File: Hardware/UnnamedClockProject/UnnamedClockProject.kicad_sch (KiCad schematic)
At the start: 22 parts, among them J101 CLOCK_OUT, J102 POWER, Q101 2N3904, U104 G3MB-202P, U105 G3MB-202P, U106 G3MB-202P

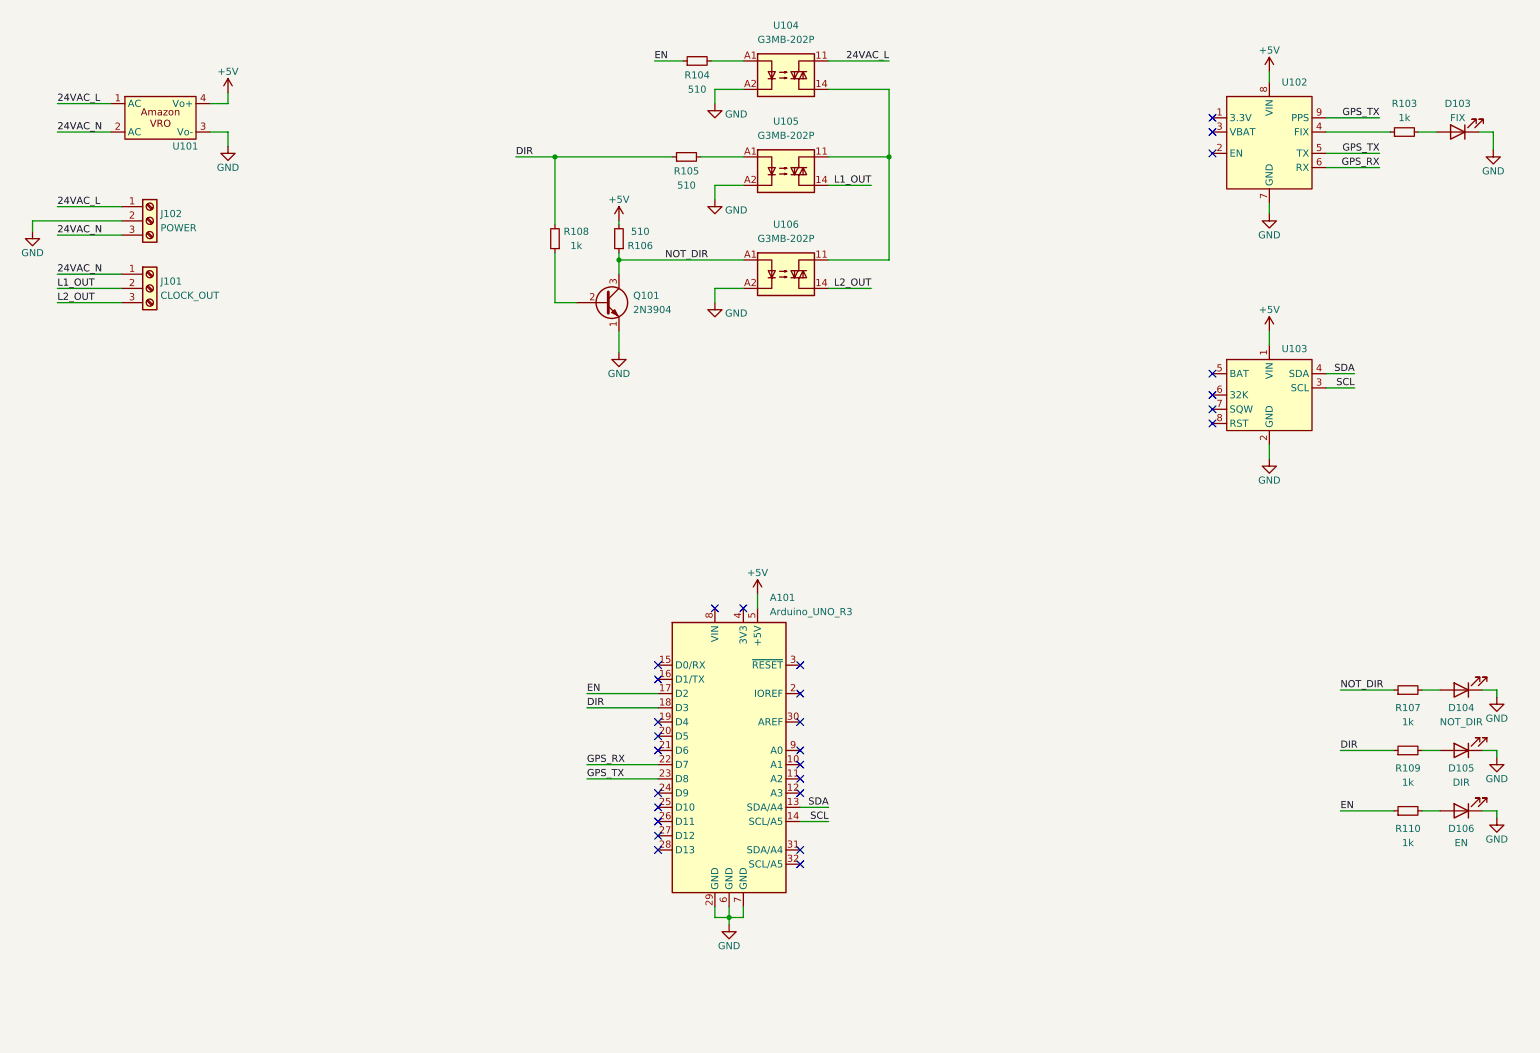
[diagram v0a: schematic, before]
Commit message: Add inital code for LCD
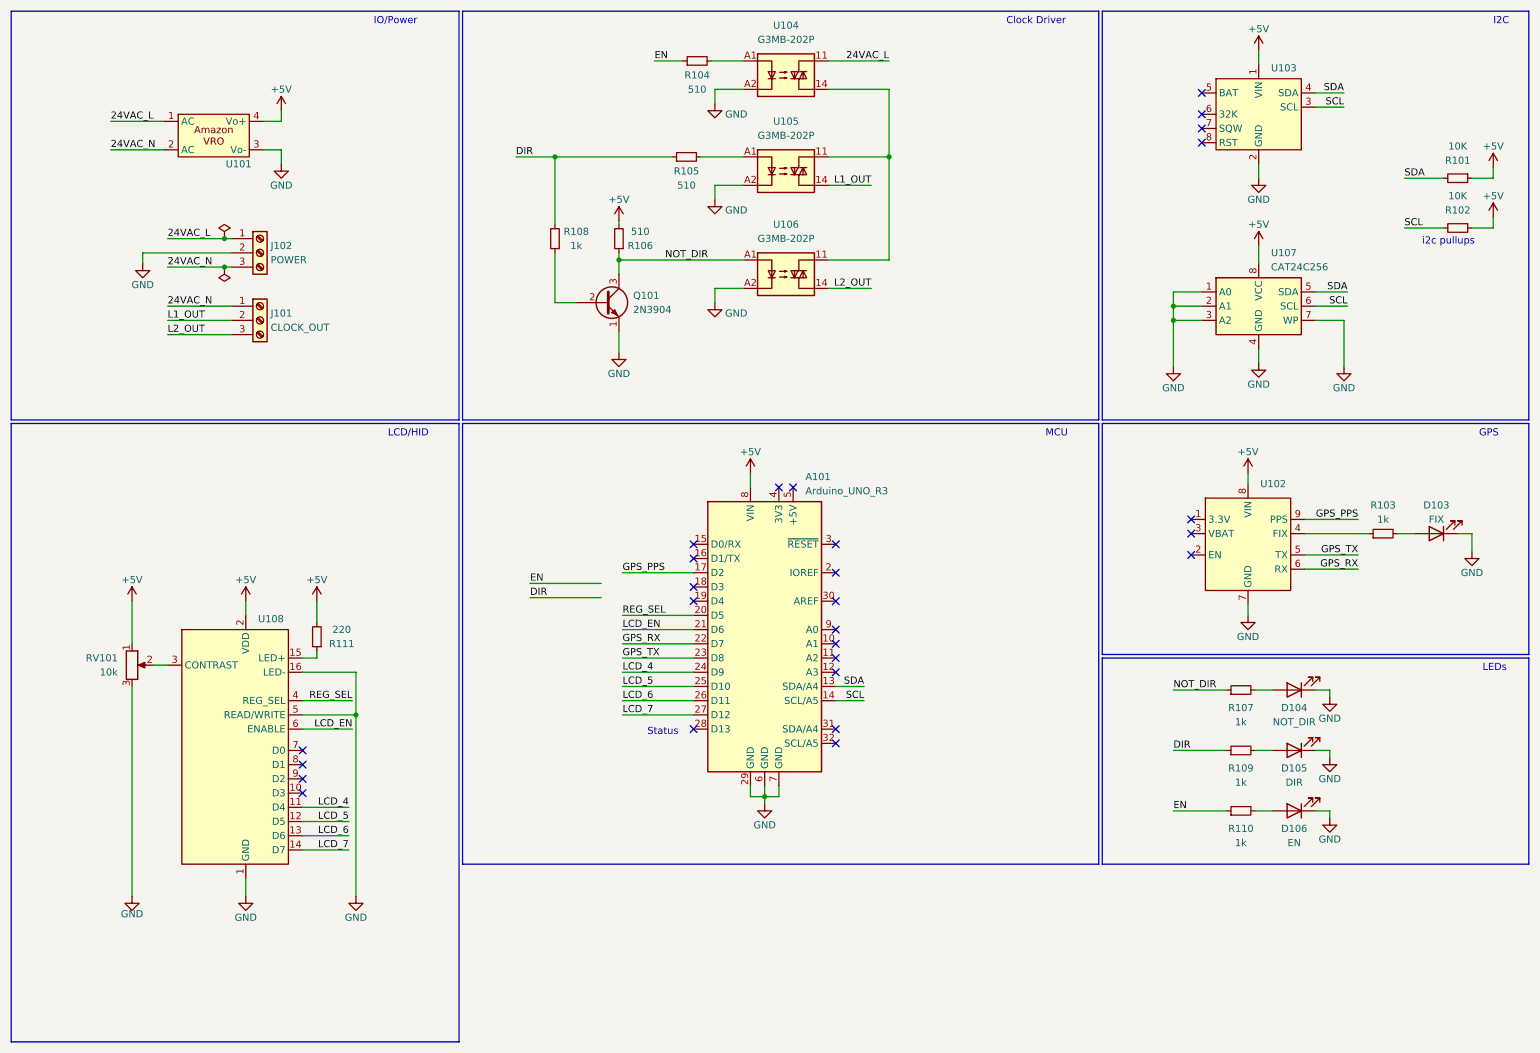
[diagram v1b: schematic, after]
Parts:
- added R101, R102: 10K, Resistor_THT:R_Axial_DIN0207_L6.3mm_D2.5mm_P10.16mm_Horizontal, symbol Device:R_Small
- added R111: 220, Resistor_THT:R_Axial_DIN0207_L6.3mm_D2.5mm_P10.16mm_Horizontal, symbol Device:R_Small
- added RV101: 10k, Potentiometer_THT:Potentiometer_Bourns_3339S_Horizontal, symbol Device:R_Potentiometer
- added U107: CAT24C256, Package_DIP:DIP-8_W7.62mm, symbol Memory_EEPROM:CAT24C256
- added U108: ~, ac1ja:2x16_LCD, symbol ac1ja:2x16_LCD
- R103, R104, R105, R106, R107, R108, R109, R110: footprint (none) -> Resistor_THT:R_Axial_DIN0207_L6.3mm_D2.5mm_P10.16mm_Horizontal
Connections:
- net +5V: now also A101.8 (VIN), R101.1, R102.1, R111.2, RV101.1, U107.8 (VCC), U108.2 (VDD); no longer A101.5 (+5V)
- net DIR: no longer A101.18 (D3)
- net EN: no longer A101.17 (D2)
- net GND: now also RV101.3, U107.1 (A0), U107.2 (A1), U107.3 (A2), U107.4 (GND), U107.7 (WP), U108.1 (GND), U108.16 (LED-), U108.5 (READ/WRITE)
- net GPS_TX: no longer U102.9 (PPS)
- net SCL: now also R102.2, U107.6 (SCL)
- net SDA: now also R101.2, U107.5 (SDA)
- net REG_SEL: now reaches A101.20 (D5)
- net REG_SEL: now also U108.4 (REG_SEL)
- net LCD_EN: now reaches A101.21 (D6)
- net LCD_EN: now also U108.6 (ENABLE)
- net LCD_4: now reaches A101.24 (D9)
- net LCD_4: now also U108.11 (D4)
- net LCD_5: now reaches A101.25 (D10)
- net LCD_5: now also U108.12 (D5)
- net LCD_6: now reaches A101.26 (D11)
- net LCD_6: now also U108.13 (D6)
- net LCD_7: now reaches A101.27 (D12)
- net LCD_7: now also U108.14 (D7)
- new net: RV101.2, U108.3 (CONTRAST)
- new net: R111.1, U108.15 (LED+)
- new net GPS_PPS: A101.17 (D2), U102.9 (PPS)
- no-connect marks 28 -> 27
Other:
- note added: "Clock Driver"
- note added: "GPS"
- note added: "I2C"
- note added: "IO/Power"
- note added: "LCD/HID"
- note added: "LEDs"
- note added: "MCU"
- note added: "Status"
- note added: "i2c pullups"
- company: (none) -> Silvertech
- title: (none) -> Unnamed Clock Project
- moved on the sheet: A101, D103, D104, D105, D106, J101, J102, R103, R107, R109, R110, U101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

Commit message: Add comments
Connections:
- net DIR: now also A101.19 (D4)
- net EN: now also A101.18 (D3)
- no-connect marks 27 -> 25
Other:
- note added: "These must also be moved in code! (EN and DIR are shift)"
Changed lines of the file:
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@@
   (no_connect (at 160.655 143.51))
   (no_connect (at 160.655 130.81))
-  (no_connect (at 135.255 115.57))
-  (no_connect (at 135.255 118.11))
   (no_connect (at 65.405 152.4))
   (no_connect (at 160.655 140.97))
@@
     (stroke (width 0) (type default))
   )
-  (wire (pts (xy 106.045 117.475) (xy 118.745 117.475))
+  (wire (pts (xy 122.555 118.11) (xy 135.255 118.11))
     (stroke (width 0) (type default))
   )
@@
     (stroke (width 0) (type default))
   )
-  (wire (pts (xy 106.045 114.935) (xy 118.745 114.935))
+  (wire (pts (xy 122.555 115.57) (xy 135.255 115.57))
     (stroke (width 0) (type default))
   )
@@
     (effects (font (size 1.27 1.27)) (justify left bottom))
   )
+  (text "These must\nalso be moved in code!\n(EN and DIR are shift)"
+    (at 98.425 118.11 0)
+    (effects (font (size 1.27 1.27)) (justify left bottom))
+  )
   (text "Status" (at 127 142.24 0)
     (effects (font (size 1.27 1.27)) (justify left bottom))
@@
     (effects (font (size 1.27 1.27)) (justify left bottom))
   )
-  (label "EN" (at 106.045 114.935 0) (fields_autoplaced)
+  (label "EN" (at 122.555 115.57 0) (fields_autoplaced)
     (effects (font (size 1.27 1.27)) (justify left bottom))
   )
@@
     (effects (font (size 1.27 1.27)) (justify right bottom))
   )
-  (label "DIR" (at 106.045 117.475 0) (fields_autoplaced)
-    (effects (font (size 1.27 1.27)) (justify left bottom))
-  )
+  (label "DIR" (at 122.555 118.11 0) (fields_autoplaced)
+    (effects (font (size 1.27 1.27)) (justify left bottom))
+  )

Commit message: Add notes
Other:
- note added: "Recomend adding a larger LED output or switched output for external lights like, need human input light."
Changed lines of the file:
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@@
+    (effects (font (size 1.27 1.27)) (justify left bottom))
+  )
+  (text "Recomend adding a larger LED\noutput or switched output for \nexternal lights like, need human\ninput light."
+    (at 169.545 152.4 0)
     (effects (font (size 1.27 1.27)) (justify left bottom))
   )

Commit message: boilerplate new pcb
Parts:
- A101: footprint Module:Arduino_UNO_R3 -> ac1ja:Arduino_Uno_Nano_Combo
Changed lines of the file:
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@@
       (effects (font (size 1.27 1.27)) (justify left))
     )
-    (property "Footprint" "Module:Arduino_UNO_R3" (at 147.955 123.19 0)
+    (property "Footprint" "ac1ja:Arduino_Uno_Nano_Combo" (at 147.955 123.19 0)
       (effects (font (size 1.27 1.27) italic) hide)
     )

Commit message: Got some work done on pcb
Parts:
- added C101: 100nF, Capacitor_THT:C_Disc_D5.0mm_W2.5mm_P5.00mm, symbol Device:C_Small
- added D101: STAT_LED, LED_THT:LED_D5.0mm, symbol Device:LED
- added D102: PWR, LED_THT:LED_D5.0mm, symbol Device:LED
- added R112, R113: 1k, Resistor_THT:R_Axial_DIN0207_L6.3mm_D2.5mm_P10.16mm_Horizontal, symbol Device:R_Small
- RV101: footprint Potentiometer_THT:Potentiometer_Bourns_3339S_Horizontal -> Potentiometer_THT:Potentiometer_Runtron_RM-065_Vertical
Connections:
- net +5V: now also C101.1, R113.1
- net GND: now also C101.2, D101.1 (K), D102.1 (K)
- net STAT: now reaches A101.28 (D13)
- net STAT: now also R112.1
- new net: D101.2 (A), R112.2
- new net: D102.2 (A), R113.2
- no-connect marks 25 -> 24
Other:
- note removed: "Status"

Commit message: Knock out a little more before class
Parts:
- added J103: BUTTONS, Connector_JST:JST_EH_B6B-EH-A_1x06_P2.50mm_Vertical, symbol Connector:Conn_01x06_Pin
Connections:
- net GND: now also J103.1 (Pin_1)
- net DN_BTN: now reaches A101.10 (A1)
- net DN_BTN: now also J103.5 (Pin_5)
- net LF_BTN: now reaches A101.11 (A2)
- net LF_BTN: now also J103.4 (Pin_4)
- net RI_BTN: now reaches A101.12 (A3)
- net RI_BTN: now also J103.3 (Pin_3)
- net MENU_BTN: now reaches A101.15 (D0/RX)
- net MENU_BTN: now also J103.2 (Pin_2)
- net UP_BTN: now reaches A101.9 (A0)
- net UP_BTN: now also J103.6 (Pin_6)
- no-connect marks 24 -> 19
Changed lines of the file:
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@@
   )
   (no_connect (at 224.155 103.505))
-  (no_connect (at 160.655 123.19))
   (no_connect (at 224.155 106.045))
   (no_connect (at 150.495 97.79))
@@
   (no_connect (at 226.06 31.115))
   (no_connect (at 160.655 113.03))
-  (no_connect (at 135.255 107.95))
-  (no_connect (at 160.655 128.27))
   (no_connect (at 226.06 27.305))
-  (no_connect (at 160.655 125.73))
   (no_connect (at 160.655 143.51))
-  (no_connect (at 160.655 130.81))
   (no_connect (at 65.405 152.4))
   (no_connect (at 160.655 140.97))
@@
     (stroke (width 0) (type default))
   )
+  (wire (pts (xy 170.18 130.81) (xy 160.655 130.81))
+    (stroke (width 0) (type default))
+  )
   (polyline (pts (xy 208.28 127.635) (xy 284.48 127.635))
     (stroke (width 0) (type default))
@@
     (stroke (width 0) (type default))
   )
+  (wire (pts (xy 194.945 106.045) (xy 199.39 106.045))
+    (stroke (width 0) (type default))
+  )
   (polyline (pts (xy 207.645 86.36) (xy 93.98 86.36))
     (stroke (width 0) (type default))
@@
     (stroke (width 0) (type default))
   )
+  (wire (pts (xy 186.69 98.425) (xy 199.39 98.425))
+    (stroke (width 0) (type default))
+  )
   (wire (pts (xy 139.065 26.67) (xy 144.145 26.67))
     (stroke (width 0) (type default))
@@
     (stroke (width 0) (type default))
   )
+  (wire (pts (xy 122.555 107.95) (xy 135.255 107.95))
+    (stroke (width 0) (type default))
+  )
   (wire (pts (xy 122.555 120.65) (xy 135.255 120.65))
     (stroke (width 0) (type default))
@@
     (stroke (width 0) (type default))
   )
-  (wire (pts (xy 160.655 133.35) (xy 165.735 133.35))
+  (wire (pts (xy 160.655 133.35) (xy 170.18 133.35))
     (stroke (width 0) (type default))
   )
@@
     (stroke (width 0) (type default))
   )
+  (wire (pts (xy 186.69 93.345) (xy 199.39 93.345))
+    (stroke (width 0) (type default))
+  )
   (wire (pts (xy 145.415 151.13) (xy 145.415 153.035))
     (stroke (width 0) (type default))
@@
     (stroke (width 0) (type default))
   )
+  (wire (pts (xy 170.18 123.19) (xy 160.655 123.19))
+    (stroke (width 0) (type default))
+  )
   (polyline (pts (xy 207.645 12.7) (xy 93.98 12.7))
     (stroke (width 0) (type default))
@@
     (stroke (width 0) (type default))
   )
+  (wire (pts (xy 186.69 103.505) (xy 199.39 103.505))
+    (stroke (width 0) (type default))
+  )
   (wire (pts (xy 31.115 37.465) (xy 40.64 37.465))
     (stroke (width 0) (type default))
@@
     (stroke (width 0) (type default))
   )
+  (wire (pts (xy 186.69 95.885) (xy 199.39 95.885))
+    (stroke (width 0) (type default))
+  )
   (wire (pts (xy 220.98 65.405) (xy 220.98 62.865))
     (stroke (width 0) (type default))
@@
     (stroke (width 0) (type default))
   )
+  (wire (pts (xy 194.945 108.585) (xy 194.945 106.045))
+    (stroke (width 0) (type default))
+  )
   (wire (pts (xy 278.13 51.435) (xy 274.32 51.435))
     (stroke (width 0) (type default))
@@
     (stroke (width 0) (type default))
   )
+  (wire (pts (xy 170.18 128.27) (xy 160.655 128.27))
+    (stroke (width 0) (type default))
+  )
   (wire (pts (xy 278.13 40.64) (xy 278.13 42.545))
     (stroke (width 0) (type default))
@@
     (stroke (width 0) (type default))
   )
-  (wire (pts (xy 160.655 135.89) (xy 165.735 135.89))
+  (wire (pts (xy 160.655 135.89) (xy 170.18 135.89))
+    (stroke (width 0) (type default))
+  )
+  (wire (pts (xy 170.18 125.73) (xy 160.655 125.73))
     (stroke (width 0) (type default))
   )
@@
   )
   (wire (pts (xy 73.66 162.56) (xy 65.405 162.56))
+    (stroke (width 0) (type default))
+  )
+  (wire (pts (xy 186.69 100.965) (xy 199.39 100.965))
     (stroke (width 0) (type default))
   )
@@
     (effects (font (size 1.27 1.27)) (justify left bottom))
   )
+  (label "RI_BTN" (at 170.18 130.81 180) (fields_autoplaced)
+    (effects (font (size 1.27 1.27)) (justify right bottom))
+  )
   (label "GPS_PPS" (at 122.555 113.03 0) (fields_autoplaced)
     (effects (font (size 1.27 1.27)) (justify left bottom))
@@
     (effects (font (size 1.27 1.27)) (justify right bottom))
   )
+  (label "DN_BTN" (at 170.18 125.73 180) (fields_autoplaced)
+    (effects (font (size 1.27 1.27)) (justify right bottom))
+  )
   (label "LCD_5" (at 73.66 157.48 180) (fields_autoplaced)
     (effects (font (size 1.27 1.27)) (justify right bottom))
@@
     (effects (font (size 1.27 1.27)) (justify right bottom))
   )
-  (label "SCL" (at 165.735 135.89 180) (fields_autoplaced)
+  (label "UP_BTN" (at 186.69 93.345 0) (fields_autoplaced)
+    (effects (font (size 1.27 1.27)) (justify left bottom))
+  )
+  (label "SCL" (at 170.18 135.89 180) (fields_autoplaced)
     (effects (font (size 1.27 1.27)) (justify right bottom))
   )
   (label "24VAC_L" (at 41.275 53.34 0) (fields_autoplaced)
+    (effects (font (size 1.27 1.27)) (justify left bottom))
+  )
+  (label "MENU_BTN" (at 122.555 107.95 0) (fields_autoplaced)
     (effects (font (size 1.27 1.27)) (justify left bottom))
   )
@@
     (effects (font (size 1.27 1.27)) (justify right bottom))
   )
+  (label "DN_BTN" (at 186.69 95.885 0) (fields_autoplaced)
+    (effects (font (size 1.27 1.27)) (justify left bottom))
+  )
   (label "REG_SEL" (at 122.555 120.65 0) (fields_autoplaced)
     (effects (font (size 1.27 1.27)) (justify left bottom))
@@
     (effects (font (size 1.27 1.27)) (justify left bottom))
   )
-  (label "SDA" (at 165.735 133.35 180) (fields_autoplaced)
+  (label "SDA" (at 170.18 133.35 180) (fields_autoplaced)
     (effects (font (size 1.27 1.27)) (justify right bottom))
   )
@@
     (effects (font (size 1.27 1.27)) (justify right bottom))
   )
+  (label "UP_BTN" (at 170.18 123.19 180) (fields_autoplaced)
+    (effects (font (size 1.27 1.27)) (justify right bottom))
+  )
   (label "24VAC_N" (at 41.275 58.42 0) (fields_autoplaced)
     (effects (font (size 1.27 1.27)) (justify left bottom))
@@
     (effects (font (size 1.27 1.27)) (justify left bottom))
   )
+  (label "RI_BTN" (at 186.69 100.965 0) (fields_autoplaced)
+    (effects (font (size 1.27 1.27)) (justify left bottom))
+  )
   (label "LCD_6" (at 122.555 135.89 0) (fields_autoplaced)
     (effects (font (size 1.27 1.27)) (justify left bottom))
@@
   (label "STAT" (at 253.365 155.575 0) (fields_autoplaced)
     (effects (font (size 1.27 1.27)) (justify left bottom))
+  )
+  (label "MENU_BTN" (at 186.69 103.505 0) (fields_autoplaced)
+    (effects (font (size 1.27 1.27)) (justify left bottom))
+  )
+  (label "LF_BTN" (at 170.18 128.27 180) (fields_autoplaced)
+    (effects (font (size 1.27 1.27)) (justify right bottom))
   )
   (label "L2_OUT" (at 167.005 62.23 180) (fields_autoplaced)
@@
   )
   (label "24VAC_N" (at 41.275 65.405 0) (fields_autoplaced)
+    (effects (font (size 1.27 1.27)) (justify left bottom))
+  )
+  (label "LF_BTN" (at 186.69 98.425 0) (fields_autoplaced)
     (effects (font (size 1.27 1.27)) (justify left bottom))
   )
@@
         (path "/c99f6c0e-9fef-4209-a089-37c9d2b153c4"
           (reference "U105") (unit 1)
+        )
+      )
+    )
+  )
+  (symbol (lib_id "Connector:Conn_01x06_Pin") (at 204.47 100.965 180) (unit 1)
+    (in_bom yes) (on_board yes) (dnp no)
+    (property "Reference" "J103" (at 198.12 107.95 0)
+      (effects (font (size 1.27 1.27)) (justify right))
+    )
+    (property "Value" "BUTTONS" (at 198.12 110.49 0)
+      (effects (font (size 1.27 1.27)) (justify right))
+    )
+    (property "Footprint" "Connector_JST:JST_EH_B6B-EH-A_1x06_P2.50mm_Vertical" (at 204.47 100.965 0)
+      (effects (font (size 1.27 1.27)) hide)
+    )
+    (property "Datasheet" "~" (at 204.47 100.965 0)
+      (effects (font (size 1.27 1.27)) hide)
+    )
+    (pin "1")
+    (pin "2")
+    (pin "3")
+    (pin "4")
+    (pin "5")
+    (pin "6")
+    (instances
+      (project "UnnamedClockProject"
+        (path "/c99f6c0e-9fef-4209-a089-37c9d2b153c4"
+          (reference "J103") (unit 1)
         )
       )
@@
         )
       )
+    )
+  )
+  (symbol (lib_id "power:GND") (at 194.945 108.585 0) (unit 1)
+    (in_bom yes) (on_board yes) (dnp no)
+    (property "Reference" "#PWR0136" (at 194.945 114.935 0)
+      (effects (font (size 1.27 1.27)) hide)
+    )
+    (property "Value" "GND" (at 194.945 112.395 0)
+      (effects (font (size 1.27 1.27)))
+    )
+    (property "Footprint" "" (at 194.945 108.585 0)
+      (effects (font (size 1.27 1.27)) hide)
+    )
+    (property "Datasheet" "" (at 194.945 108.585 0)
+      (effects (font (size 1.27 1.27)) hide)
+    )
+    (pin "1")
+    (instances
+      (project "UnnamedClockProject"
+        (path "/c99f6c0e-9fef-4209-a089-37c9d2b153c4"
+          (reference "#PWR0136") (unit 1)
+        )
+      )
